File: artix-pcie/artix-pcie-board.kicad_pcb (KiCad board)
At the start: 2 copper layers, 2 parts, among them U1 xc7a15tfgg484, U2 TOFE-4X

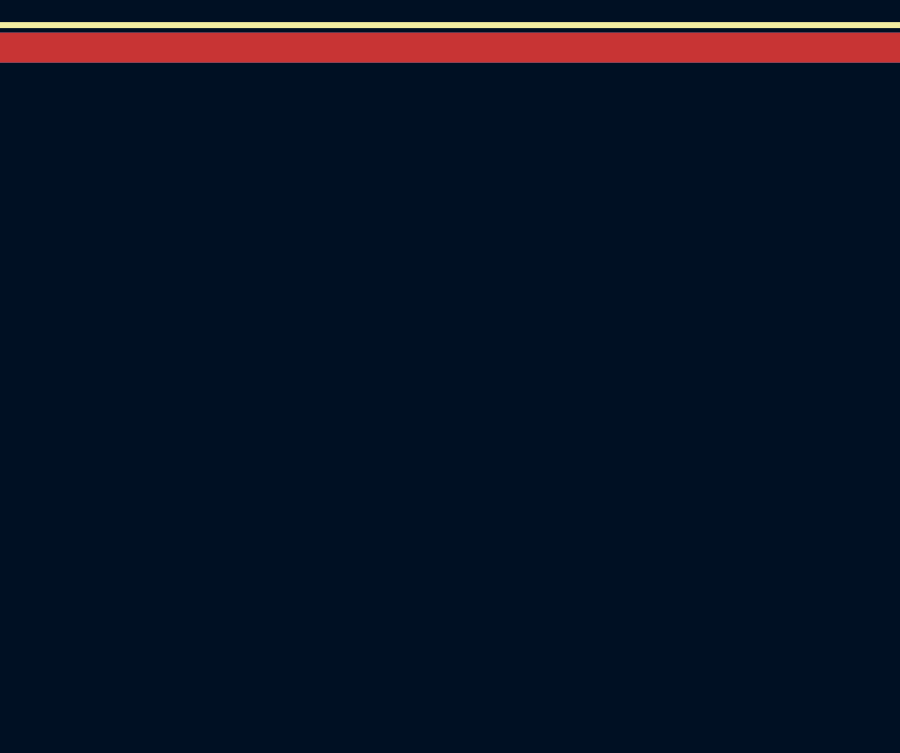
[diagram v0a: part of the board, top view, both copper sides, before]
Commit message: added qspi flash. need jtag connector next
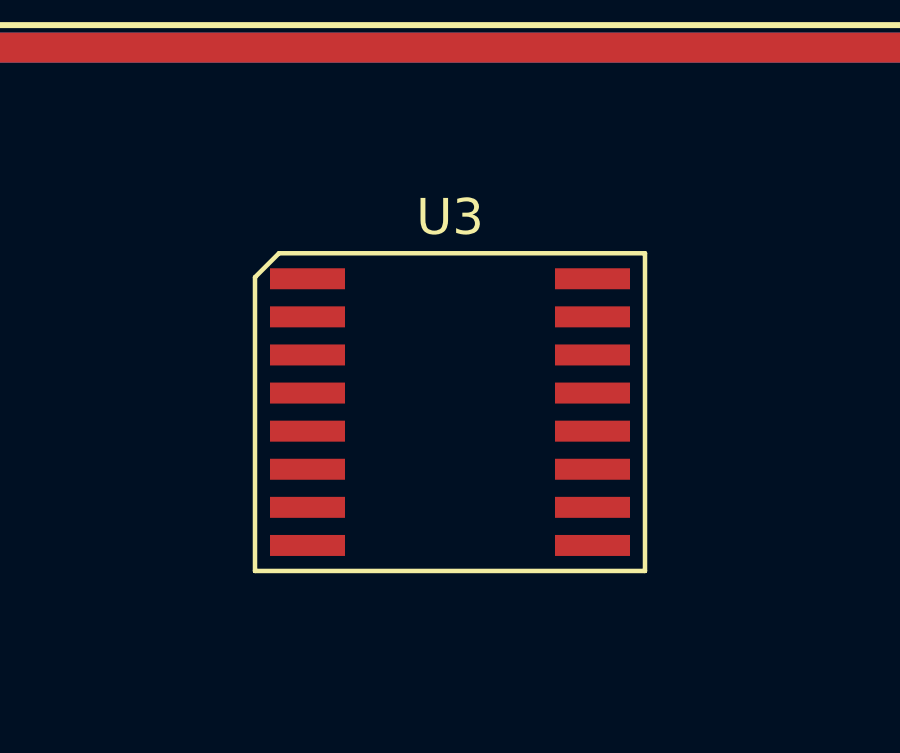
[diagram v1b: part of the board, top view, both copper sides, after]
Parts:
- added U3: N25Q256_QSPI, footlib:micron_SOP2-16, F.Cu at (112.2, 73.4)
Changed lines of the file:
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@@
     (links 207)
     (no_connects 202)
-    (area 51.623 60.272999 131.477001 129.727001)
+    (area 0 0 0 0)
     (thickness 1.6)
     (drawings 0)
     (tracks 0)
     (zones 0)
-    (modules 2)
-    (nets 342)
+    (modules 3)
+    (nets 358)
   )
   (page A4)
@@
   (net 340 "Net-(U1-PadY22)")
   (net 341 "Net-(U1-PadAB22)")
+  (net 342 "Net-(U3-Pad16)")
+  (net 343 "Net-(U3-Pad1)")
+  (net 344 "Net-(U3-Pad15)")
+  (net 345 "Net-(U3-Pad2)")
+  (net 346 "Net-(U3-Pad14)")
+  (net 347 "Net-(U3-Pad3)")
+  (net 348 "Net-(U3-Pad13)")
+  (net 349 "Net-(U3-Pad4)")
+  (net 350 "Net-(U3-Pad12)")
+  (net 351 "Net-(U3-Pad5)")
+  (net 352 "Net-(U3-Pad11)")
+  (net 353 "Net-(U3-Pad6)")
+  (net 354 "Net-(U3-Pad10)")
+  (net 355 "Net-(U3-Pad7)")
+  (net 356 "Net-(U3-Pad9)")
+  (net 357 "Net-(U3-Pad8)")
   (net_class Default "This is the default net class."
     (clearance 0.127)
@@
     (add_net "Net-(U2-PadB6)")
     (add_net "Net-(U2-PadB9)")
+    (add_net "Net-(U3-Pad1)")
+    (add_net "Net-(U3-Pad10)")
+    (add_net "Net-(U3-Pad11)")
+    (add_net "Net-(U3-Pad12)")
+    (add_net "Net-(U3-Pad13)")
+    (add_net "Net-(U3-Pad14)")
+    (add_net "Net-(U3-Pad15)")
+    (add_net "Net-(U3-Pad16)")
+    (add_net "Net-(U3-Pad2)")
+    (add_net "Net-(U3-Pad3)")
+    (add_net "Net-(U3-Pad4)")
+    (add_net "Net-(U3-Pad5)")
+    (add_net "Net-(U3-Pad6)")
+    (add_net "Net-(U3-Pad7)")
+    (add_net "Net-(U3-Pad8)")
+    (add_net "Net-(U3-Pad9)")
   )
   (module TOFE_4X_HalfHeight (layer F.Cu)
@@
       (net 341 "Net-(U1-PadAB22)") (solder_mask_margin 0.05))
   )
+  (module footlib:micron_SOP2-16 (layer F.Cu)
+    (at 112.2 73.4 270)
+    (fp_text reference U3 (at -6.495 0 360) (layer F.SilkS)
+      (effects (font (size 1.2 1.2) (thickness 0.15)))
+    )
+    (fp_text value N25Q256_QSPI (at 6.4 0.1 360) (layer F.Fab)
+      (effects (font (size 1.2 1.2) (thickness 0.15)))
+    )
+    (fp_line (start -4.495 6.5) (end -5.295 5.7) (layer F.SilkS) (width 0.15))
+    (fp_line (start -5.295 5.7) (end -5.295 -6.5) (layer F.SilkS) (width 0.15))
+    (fp_line (start -5.295 -6.5) (end 5.295 -6.5) (layer F.SilkS) (width 0.15))
+    (fp_line (start 5.295 -6.5) (end 5.295 6.5) (layer F.SilkS) (width 0.15))
+    (fp_line (start 5.295 6.5) (end -4.495 6.5) (layer F.SilkS) (width 0.15))
+    (pad 16 smd rect (at -4.445 -4.75 270) (size 0.7 2.5) (layers F.Cu F.Paste F.Mask)
+      (net 342 "Net-(U3-Pad16)"))
+    (pad 1 smd rect (at -4.445 4.75 270) (size 0.7 2.5) (layers F.Cu F.Paste F.Mask)
+      (net 343 "Net-(U3-Pad1)"))
+    (pad 15 smd rect (at -3.175 -4.75 270) (size 0.7 2.5) (layers F.Cu F.Paste F.Mask)
+      (net 344 "Net-(U3-Pad15)"))
+    (pad 2 smd rect (at -3.175 4.75 270) (size 0.7 2.5) (layers F.Cu F.Paste F.Mask)
+      (net 345 "Net-(U3-Pad2)"))
+    (pad 14 smd rect (at -1.905 -4.75 270) (size 0.7 2.5) (layers F.Cu F.Paste F.Mask)
+      (net 346 "Net-(U3-Pad14)"))
+    (pad 3 smd rect (at -1.905 4.75 270) (size 0.7 2.5) (layers F.Cu F.Paste F.Mask)
+      (net 347 "Net-(U3-Pad3)"))
+    (pad 13 smd rect (at -0.635 -4.75 270) (size 0.7 2.5) (layers F.Cu F.Paste F.Mask)
+      (net 348 "Net-(U3-Pad13)"))
+    (pad 4 smd rect (at -0.635 4.75 270) (size 0.7 2.5) (layers F.Cu F.Paste F.Mask)
+      (net 349 "Net-(U3-Pad4)"))
+    (pad 12 smd rect (at 0.635 -4.75 270) (size 0.7 2.5) (layers F.Cu F.Paste F.Mask)
+      (net 350 "Net-(U3-Pad12)"))
+    (pad 5 smd rect (at 0.635 4.75 270) (size 0.7 2.5) (layers F.Cu F.Paste F.Mask)
+      (net 351 "Net-(U3-Pad5)"))
+    (pad 11 smd rect (at 1.905 -4.75 270) (size 0.7 2.5) (layers F.Cu F.Paste F.Mask)
+      (net 352 "Net-(U3-Pad11)"))
+    (pad 6 smd rect (at 1.905 4.75 270) (size 0.7 2.5) (layers F.Cu F.Paste F.Mask)
+      (net 353 "Net-(U3-Pad6)"))
+    (pad 10 smd rect (at 3.175 -4.75 270) (size 0.7 2.5) (layers F.Cu F.Paste F.Mask)
+      (net 354 "Net-(U3-Pad10)"))
+    (pad 7 smd rect (at 3.175 4.75 270) (size 0.7 2.5) (layers F.Cu F.Paste F.Mask)
+      (net 355 "Net-(U3-Pad7)"))
+    (pad 9 smd rect (at 4.445 -4.75 270) (size 0.7 2.5) (layers F.Cu F.Paste F.Mask)
+      (net 356 "Net-(U3-Pad9)"))
+    (pad 8 smd rect (at 4.445 4.75 270) (size 0.7 2.5) (layers F.Cu F.Paste F.Mask)
+      (net 357 "Net-(U3-Pad8)"))
+  )
 )

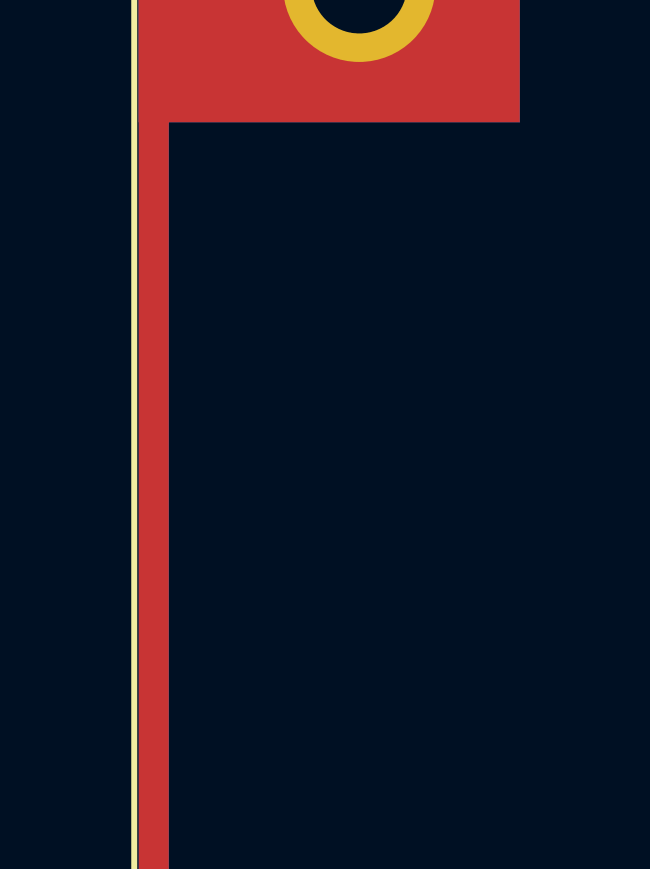
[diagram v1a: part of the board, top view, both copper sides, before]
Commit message: added jtag connector. consider CSG325 17x17mm package
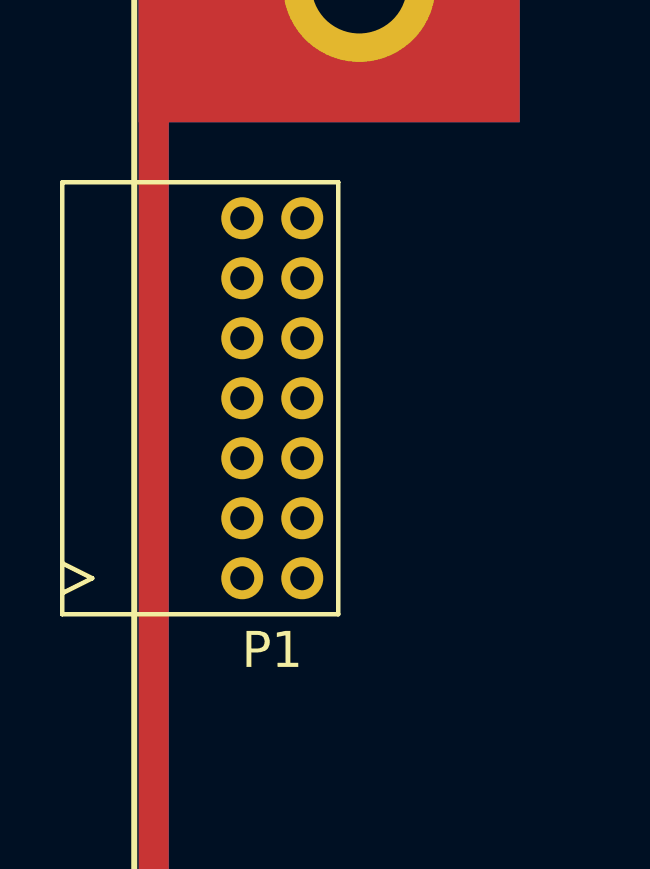
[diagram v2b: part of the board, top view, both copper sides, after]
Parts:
- added P1: JTAG_CONN, footlib:JTAG_RA, F.Cu at (56.6, 80.0)
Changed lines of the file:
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@@
     (tracks 0)
     (zones 0)
-    (modules 3)
-    (nets 358)
+    (modules 4)
+    (nets 372)
   )
   (page A4)
@@
   (net 356 "Net-(U3-Pad9)")
   (net 357 "Net-(U3-Pad8)")
+  (net 358 "Net-(P1-Pad2)")
+  (net 359 "Net-(P1-Pad1)")
+  (net 360 "Net-(P1-Pad4)")
+  (net 361 "Net-(P1-Pad3)")
+  (net 362 "Net-(P1-Pad6)")
+  (net 363 "Net-(P1-Pad5)")
+  (net 364 "Net-(P1-Pad8)")
+  (net 365 "Net-(P1-Pad7)")
+  (net 366 "Net-(P1-Pad10)")
+  (net 367 "Net-(P1-Pad9)")
+  (net 368 "Net-(P1-Pad12)")
+  (net 369 "Net-(P1-Pad11)")
+  (net 370 "Net-(P1-Pad14)")
+  (net 371 "Net-(P1-Pad13)")
   (net_class Default "This is the default net class."
     (clearance 0.127)
@@
     (add_net /GND)
     (add_net /V2_5)
+    (add_net "Net-(P1-Pad1)")
+    (add_net "Net-(P1-Pad10)")
+    (add_net "Net-(P1-Pad11)")
+    (add_net "Net-(P1-Pad12)")
+    (add_net "Net-(P1-Pad13)")
+    (add_net "Net-(P1-Pad14)")
+    (add_net "Net-(P1-Pad2)")
+    (add_net "Net-(P1-Pad3)")
+    (add_net "Net-(P1-Pad4)")
+    (add_net "Net-(P1-Pad5)")
+    (add_net "Net-(P1-Pad6)")
+    (add_net "Net-(P1-Pad7)")
+    (add_net "Net-(P1-Pad8)")
+    (add_net "Net-(P1-Pad9)")
     (add_net "Net-(U1-PadA1)")
     (add_net "Net-(U1-PadA10)")
@@
       (net 357 "Net-(U3-Pad8)"))
   )
+  (module footlib:JTAG_RA (layer F.Cu)
+    (at 56.6 80 90)
+    (fp_text reference P1 (at -8.4 0 180) (layer F.SilkS)
+      (effects (font (size 1.2 1.2) (thickness 0.15)))
+    )
+    (fp_text value JTAG_CONN (at 0 -3.9 90) (layer F.Fab)
+      (effects (font (size 1.2 1.2) (thickness 0.15)))
+    )
+    (fp_line (start -5.5 -7) (end -6 -6) (layer F.SilkS) (width 0.15))
+    (fp_line (start -6.5 -7) (end -6 -6) (layer F.SilkS) (width 0.15))
+    (fp_line (start -7.2 2.199999) (end 7.2 2.2) (layer F.SilkS) (width 0.15))
+    (fp_line (start 7.2 2.2) (end 7.2 -7) (layer F.SilkS) (width 0.15))
+    (fp_line (start 7.2 -7) (end -7.2 -7) (layer F.SilkS) (width 0.15))
+    (fp_line (start -7.2 -7) (end -7.2 2.2) (layer F.SilkS) (width 0.15))
+    (pad 2 thru_hole circle (at -6 -1 90) (size 1.4 1.4) (drill 0.8) (layers *.Cu *.Mask F.SilkS)
+      (net 358 "Net-(P1-Pad2)"))
+    (pad 1 thru_hole circle (at -6 1 90) (size 1.4 1.4) (drill 0.8) (layers *.Cu *.Mask F.SilkS)
+      (net 359 "Net-(P1-Pad1)"))
+    (pad 4 thru_hole circle (at -4 -1 90) (size 1.4 1.4) (drill 0.8) (layers *.Cu *.Mask F.SilkS)
+      (net 360 "Net-(P1-Pad4)"))
+    (pad 3 thru_hole circle (at -4 1 90) (size 1.4 1.4) (drill 0.8) (layers *.Cu *.Mask F.SilkS)
+      (net 361 "Net-(P1-Pad3)"))
+    (pad 6 thru_hole circle (at -2 -1 90) (size 1.4 1.4) (drill 0.8) (layers *.Cu *.Mask F.SilkS)
+      (net 362 "Net-(P1-Pad6)"))
+    (pad 5 thru_hole circle (at -2 1 90) (size 1.4 1.4) (drill 0.8) (layers *.Cu *.Mask F.SilkS)
+      (net 363 "Net-(P1-Pad5)"))
+    (pad 8 thru_hole circle (at 0 -1 90) (size 1.4 1.4) (drill 0.8) (layers *.Cu *.Mask F.SilkS)
+      (net 364 "Net-(P1-Pad8)"))
+    (pad 7 thru_hole circle (at 0 1 90) (size 1.4 1.4) (drill 0.8) (layers *.Cu *.Mask F.SilkS)
+      (net 365 "Net-(P1-Pad7)"))
+    (pad 10 thru_hole circle (at 2 -1 90) (size 1.4 1.4) (drill 0.8) (layers *.Cu *.Mask F.SilkS)
+      (net 366 "Net-(P1-Pad10)"))
+    (pad 9 thru_hole circle (at 2 1 90) (size 1.4 1.4) (drill 0.8) (layers *.Cu *.Mask F.SilkS)
+      (net 367 "Net-(P1-Pad9)"))
+    (pad 12 thru_hole circle (at 4 -1 90) (size 1.4 1.4) (drill 0.8) (layers *.Cu *.Mask F.SilkS)
+      (net 368 "Net-(P1-Pad12)"))
+    (pad 11 thru_hole circle (at 4 1 90) (size 1.4 1.4) (drill 0.8) (layers *.Cu *.Mask F.SilkS)
+      (net 369 "Net-(P1-Pad11)"))
+    (pad 14 thru_hole circle (at 6 -1 90) (size 1.4 1.4) (drill 0.8) (layers *.Cu *.Mask F.SilkS)
+      (net 370 "Net-(P1-Pad14)"))
+    (pad 13 thru_hole circle (at 6 1 90) (size 1.4 1.4) (drill 0.8) (layers *.Cu *.Mask F.SilkS)
+      (net 371 "Net-(P1-Pad13)"))
+  )
 )

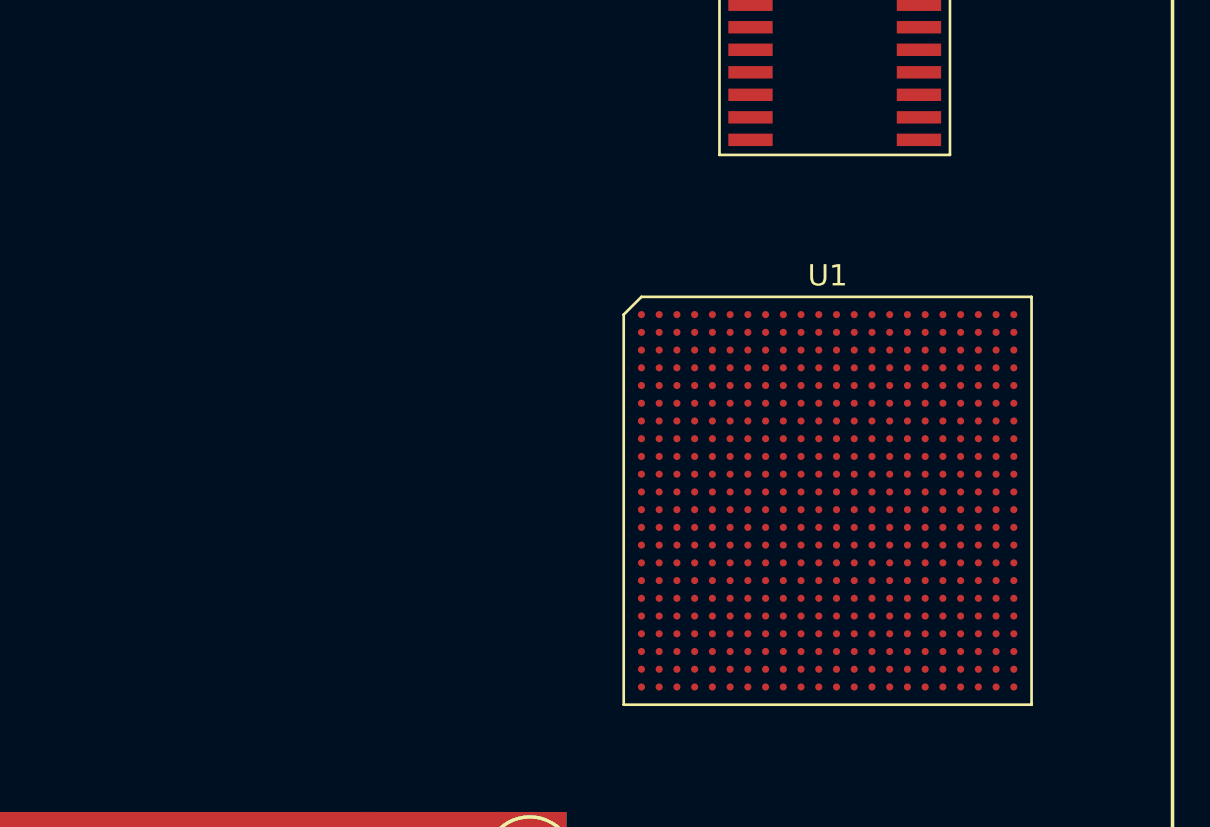
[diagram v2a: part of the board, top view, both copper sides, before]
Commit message: working on 0.8mm BGA problem
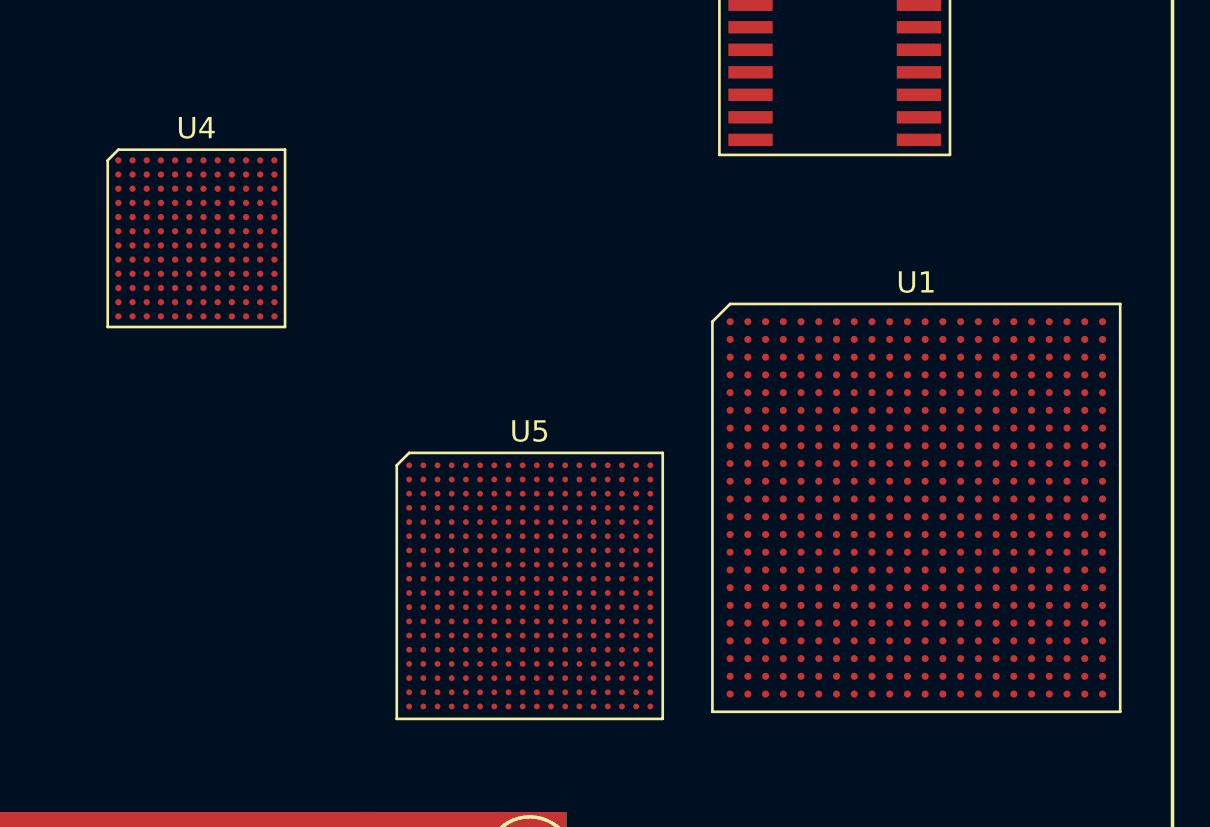
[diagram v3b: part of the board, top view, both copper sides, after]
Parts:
- added U4: AD9361, footlib:AD9361, F.Cu at (76.2, 83.4)
- added U5: xc7a15tcsg325, footlib:Xil_Artix_CSG325, F.Cu at (95.0, 103.0)
- moved U1 5.02 mm to (116.8, 98.6)
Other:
- net class Default: clearance 0.127 -> 0.1016; trace_width 0.127 -> 0.1016; via_dia 0.6096 -> 0.495
- rule trace_clearance: 0.127 -> 0.1016
- rule trace_min: 0.127 -> 0.1016
- rule via_min_size: 0.6096 -> 0.495
